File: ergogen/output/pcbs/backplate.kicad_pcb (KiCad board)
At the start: 2 copper layers, 133.8 x 88.1 mm, 5 parts

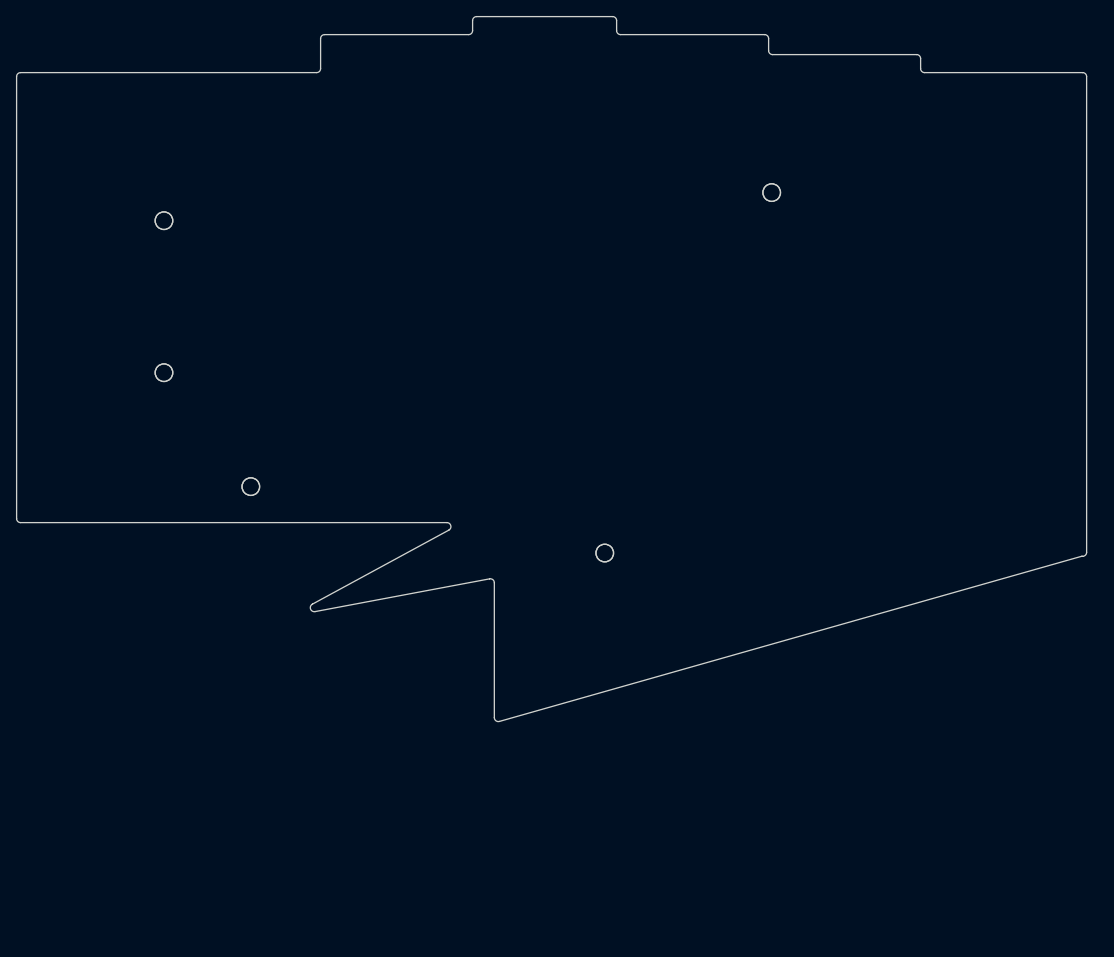
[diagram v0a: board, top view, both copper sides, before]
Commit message: feat: souffle outputs
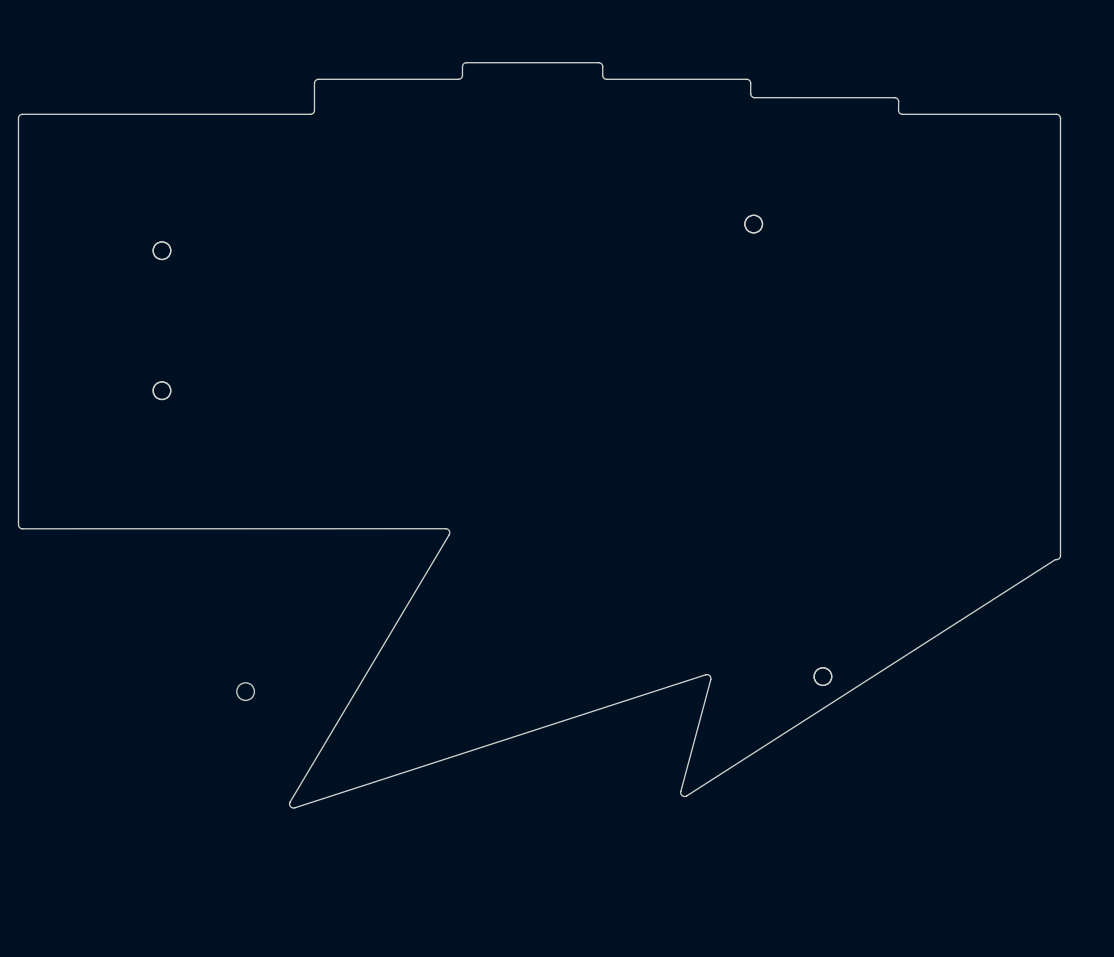
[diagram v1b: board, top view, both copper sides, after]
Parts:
- moved MH5 31.3 mm to (191.9, 109.5), turned to -15 degrees
- moved MH4 25.6 mm to (119.7, 111.4)
- moved MH3 4.54 mm to (183.2, 52.9)
- moved MH1 3.76 mm to (109.2, 56.2)
- moved MH2 2.26 mm to (109.2, 73.8)
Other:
- board size 133.8 x 88.1 mm -> 130.3 x 93.2 mm

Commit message: fix: number row on top and improved outline
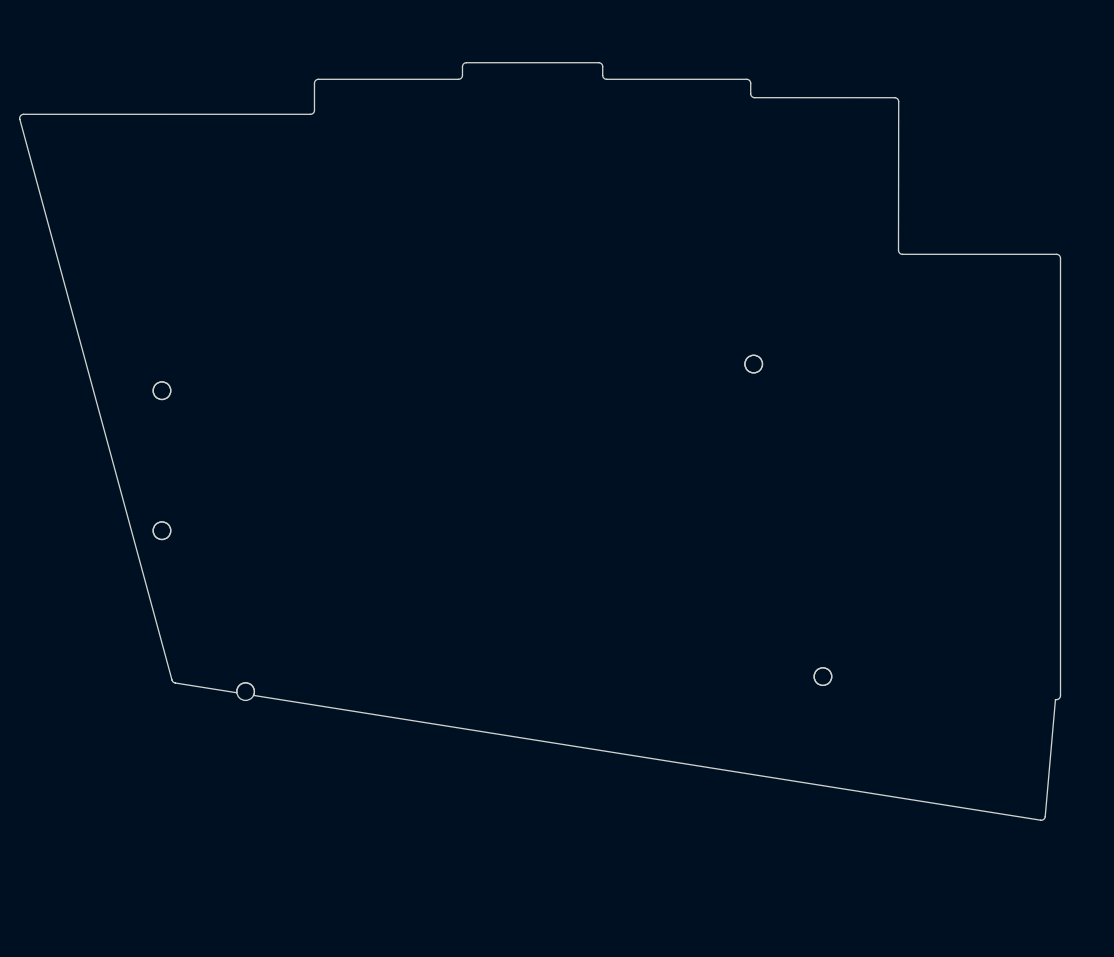
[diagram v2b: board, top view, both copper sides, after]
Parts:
- moved MH3 17.5 mm to (183.2, 70.4)
- moved MH1 17.5 mm to (109.2, 73.8)
- moved MH2 17.5 mm to (109.2, 91.2)
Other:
- board size 130.3 x 93.2 mm -> 130.1 x 94.7 mm
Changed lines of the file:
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@@
   (footprint "ceoloide:mounting_hole_npth"
     (layer "F.Cu")
-    (at 109.25 56.25 0)
+    (at 109.25 73.75 0)
     (property "Reference" "MH1"
       (at 0 2.55 0)
@@
   (footprint "ceoloide:mounting_hole_npth"
     (layer "F.Cu")
-    (at 109.25 73.75 0)
+    (at 109.25 91.25 0)
     (property "Reference" "MH2"
       (at 0 2.55 0)
@@
   (footprint "ceoloide:mounting_hole_npth"
     (layer "F.Cu")
-    (at 183.218 52.9235 0)
+    (at 183.218 70.4235 0)
     (property "Reference" "MH3"
       (at 0 2.55 0)
@@
     )
   )
-  (gr_line (start 91.3169806967852 90.51245022052899) (end 91.31501930151654 39.70250578597188) (layer Edge.Cuts) (stroke (width 0.15) (type default)))
-(gr_line (start 91.81500580151655 39.20248648632969) (end 127.8150135 39.20151351314865) (layer Edge.Cuts) (stroke (width 0.15) (type default)))
-(gr_line (start 128.315 38.70151351314865) (end 128.315 35.3275) (layer Edge.Cuts) (stroke (width 0.15) (type default)))
+  (gr_line (start 110.50826649856596 109.92527651860325) (end 91.48622889852672 39.83343914341975) (layer Edge.Cuts) (stroke (width 0.15) (type default)))
+(gr_line (start 91.9687610950968 39.202482330781216) (end 127.8150135 39.201513513148655) (layer Edge.Cuts) (stroke (width 0.15) (type default)))
+(gr_line (start 128.315 38.701513513148655) (end 128.315 35.3275) (layer Edge.Cuts) (stroke (width 0.15) (type default)))
 (gr_line (start 128.815 34.8275) (end 146.315 34.8275) (layer Edge.Cuts) (stroke (width 0.15) (type default)))
 (gr_line (start 146.815 34.3275) (end 146.815 33.2525) (layer Edge.Cuts) (stroke (width 0.15) (type default)))
@@
 (gr_line (start 164.843 34.8275) (end 182.343 34.8275) (layer Edge.Cuts) (stroke (width 0.15) (type default)))
 (gr_line (start 182.843 35.3275) (end 182.843 36.62312159204324) (layer Edge.Cuts) (stroke (width 0.15) (type default)))
-(gr_line (start 183.34287840000002 37.12312159204324) (end 200.83706271163646 37.1273769341731) (layer Edge.Cuts) (stroke (width 0.15) (type default)))
-(gr_line (start 201.3369048122388 37.63340058417816) (end 201.32409667048205 38.6964763499891) (layer Edge.Cuts) (stroke (width 0.15) (type default)))
-(gr_line (start 220.93800000000002 94.8635) (end 174.86233811395525 124.39610377258694) (layer Edge.Cuts) (stroke (width 0.15) (type default)))
-(gr_line (start 174.1095621012308 123.84574198074279) (end 177.85461254469791 109.86902346027989) (layer Edge.Cuts) (stroke (width 0.15) (type default)))
-(gr_line (start 177.21764863004648 109.26392106502323) (end 125.85741047443018 125.89130668921796) (layer Edge.Cuts) (stroke (width 0.15) (type default)))
-(gr_line (start 125.27378216867217 125.15983977902275) (end 145.15748568914685 91.76089554320336) (layer Edge.Cuts) (stroke (width 0.15) (type default)))
-(gr_line (start 144.7277893480403 91.00512152825797) (end 91.8170497467852 91.01243092026964) (layer Edge.Cuts) (stroke (width 0.15) (type default)))
-(gr_line (start 201.82406037108433 39.2025) (end 221.068 39.2025) (layer Edge.Cuts) (stroke (width 0.15) (type default)))
-(gr_line (start 221.568 39.7025) (end 221.568 94.3635) (layer Edge.Cuts) (stroke (width 0.15) (type default)))
-(gr_line (start 221.068 94.8635) (end 220.93800000000002 94.8635) (layer Edge.Cuts) (stroke (width 0.15) (type default)))
-(gr_arc (start 91.81500580151655 39.202486486174166) (mid 91.46145430151654 39.348944686174164) (end 91.31501930151654 39.702505786174164) (layer Edge.Cuts) (stroke (width 0.15) (type default)))
-(gr_arc (start 127.81501349999999 39.20151351314865) (mid 128.1685582 39.05506211314865) (end 128.315 38.70151351314865) (layer Edge.Cuts) (stroke (width 0.15) (type default)))
+(gr_line (start 183.34287840000002 37.12312159204324) (end 200.8424827703032 37.12737825256575) (layer Edge.Cuts) (stroke (width 0.15) (type default)))
+(gr_line (start 201.34236077036712 37.628016802540515) (end 201.31863938512134 56.201861450012075) (layer Edge.Cuts) (stroke (width 0.15) (type default)))
+(gr_line (start 220.93800000000002 112.3635) (end 219.65752596395185 126.98539423067496) (layer Edge.Cuts) (stroke (width 0.15) (type default)))
+(gr_line (start 219.08114720800037 127.43560839237159) (end 120.6993432 111.83961029999999) (layer Edge.Cuts) (stroke (width 0.15) (type default)))
+(gr_line (start 118.6165232 111.50943079999999) (end 110.91252714391037 110.28815311369672) (layer Edge.Cuts) (stroke (width 0.15) (type default)))
+(gr_line (start 201.81863898518517 56.7025) (end 221.068 56.7025) (layer Edge.Cuts) (stroke (width 0.15) (type default)))
+(gr_line (start 221.568 57.2025) (end 221.568 111.8635) (layer Edge.Cuts) (stroke (width 0.15) (type default)))
+(gr_line (start 221.068 112.3635) (end 220.93800000000002 112.3635) (layer Edge.Cuts) (stroke (width 0.15) (type default)))
+(gr_arc (start 91.9687610950968 39.20248233078121) (mid 91.5716065950968 39.39874303078121) (end 91.48622889509679 39.83343913078121) (layer Edge.Cuts) (stroke (width 0.15) (type default)))
+(gr_arc (start 127.81501349999999 39.201513513148655) (mid 128.1685582 39.05506211314866) (end 128.315 38.701513513148655) (layer Edge.Cuts) (stroke (width 0.15) (type default)))
 (gr_arc (start 128.815 34.8275) (mid 128.4614466 34.9739466) (end 128.315 35.3275) (layer Edge.Cuts) (stroke (width 0.15) (type default)))
 (gr_arc (start 146.315 34.8275) (mid 146.6685534 34.6810534) (end 146.815 34.3275) (layer Edge.Cuts) (stroke (width 0.15) (type default)))
@@
 (gr_arc (start 182.843 35.3275) (mid 182.6965534 34.9739466) (end 182.343 34.8275) (layer Edge.Cuts) (stroke (width 0.15) (type default)))
 (gr_arc (start 182.843 36.62312159204324) (mid 182.9894036 36.97663199204324) (end 183.3428784 37.12312159204324) (layer Edge.Cuts) (stroke (width 0.15) (type default)))
-(gr_arc (start 201.33690481163643 37.6334006341731) (mid 201.19266061163643 37.2760029341731) (end 200.83706271163643 37.1273769341731) (layer Edge.Cuts) (stroke (width 0.15) (type default)))
-(gr_arc (start 201.32409667108433 38.69647629999942) (mid 201.46838367108433 39.05391719999942) (end 201.82406037108433 39.20249999999942) (layer Edge.Cuts) (stroke (width 0.15) (type default)))
-(gr_arc (start 221.568 39.7025) (mid 221.42155340000002 39.3489466) (end 221.068 39.2025) (layer Edge.Cuts) (stroke (width 0.15) (type default)))
-(gr_arc (start 221.068 94.8635) (mid 221.42155340000002 94.7170534) (end 221.568 94.3635) (layer Edge.Cuts) (stroke (width 0.15) (type default)))
-(gr_arc (start 174.10956210123078 123.84574198074284) (mid 174.29742720123076 124.37878158074284) (end 174.86233810123076 124.39610378074283) (layer Edge.Cuts) (stroke (width 0.15) (type default)))
-(gr_arc (start 177.85461254469791 109.86902346027993) (mid 177.71602034469794 109.37711046027994) (end 177.21764864469793 109.26392116027993) (layer Edge.Cuts) (stroke (width 0.15) (type default)))
-(gr_arc (start 125.27378215977875 125.15983979396121) (mid 125.31257265977875 125.72745759396122) (end 125.85741045977875 125.89130659396122) (layer Edge.Cuts) (stroke (width 0.15) (type default)))
-(gr_arc (start 145.1574856980403 91.76089552826491) (mid 145.1625175980403 91.2579954282649) (end 144.7277892980403 91.00512152826491) (layer Edge.Cuts) (stroke (width 0.15) (type default)))
-(gr_arc (start 91.3169806967852 90.51245022026274) (mid 91.4634584967852 90.86601552026274) (end 91.81704969678519 91.01243092026273) (layer Edge.Cuts) (stroke (width 0.15) (type default)))
-(gr_circle (center 109.25 56.25) (end 110.35 56.25) (layer Edge.Cuts) (stroke (width 0.15) (type default)) (fill none))
+(gr_arc (start 201.3423607703032 37.62801675256575) (mid 201.19618317030321 37.274093652565746) (end 200.8424827703032 37.12737825256575) (layer Edge.Cuts) (stroke (width 0.15) (type default)))
+(gr_arc (start 201.31863938518518 56.20186150001397) (mid 201.46485988518518 56.55582760001397) (end 201.81863908518517 56.70250000001397) (layer Edge.Cuts) (stroke (width 0.15) (type default)))
+(gr_arc (start 221.568 57.2025) (mid 221.42155340000002 56.8489466) (end 221.068 56.7025) (layer Edge.Cuts) (stroke (width 0.15) (type default)))
+(gr_arc (start 221.068 112.3635) (mid 221.42155340000002 112.2170534) (end 221.568 111.8635) (layer Edge.Cuts) (stroke (width 0.15) (type default)))
+(gr_arc (start 219.08114715922605 127.43560838463978) (mid 219.46721955922604 127.33581428463978) (end 219.65752595922604 126.98539428463978) (layer Edge.Cuts) (stroke (width 0.15) (type default)))
+(gr_arc (start 110.50826649513606 109.92527650596477) (mid 110.65681719513606 110.16640490596477) (end 110.91252709513606 110.28815320596476) (layer Edge.Cuts) (stroke (width 0.15) (type default)))
 (gr_circle (center 109.25 73.75) (end 110.35 73.75) (layer Edge.Cuts) (stroke (width 0.15) (type default)) (fill none))
-(gr_circle (center 183.218 52.9235) (end 184.31799999999998 52.9235) (layer Edge.Cuts) (stroke (width 0.15) (type default)) (fill none))
+(gr_circle (center 109.25 91.25) (end 110.35 91.25) (layer Edge.Cuts) (stroke (width 0.15) (type default)) (fill none))
+(gr_circle (center 183.218 70.4235) (end 184.31799999999998 70.4235) (layer Edge.Cuts) (stroke (width 0.15) (type default)) (fill none))
+(gr_arc (start 120.6993432 111.83961029999999) (mid 119.87922710000001 110.2785665) (end 118.6165232 111.50943079999999) (layer Edge.Cuts) (stroke (width 0.15) (type default)))
 (gr_circle (center 191.871694 109.48666770000001) (end 192.97169399999999 109.48666770000001) (layer Edge.Cuts) (stroke (width 0.15) (type default)) (fill none))
 )
